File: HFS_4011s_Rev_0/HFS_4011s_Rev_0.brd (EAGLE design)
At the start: 47 x 44.5 mm, 15 parts, among them IC1 CP2104, J1 2X06, J2 2X12, Q1 mmbt2222, Q2 mmbt2222, SW2 KMR2, X2 ESP32_WROOM32_SKINNY, X4 20329

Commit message: Added power circuitry to board. Using 5V buck boost and 3.3V LDO. Added 1x02 pin header for on-off switch.
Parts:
- added B1: 1.8-5V, microbuilder:JSTPH2
- added C1: 10uF, microbuilder:0805-NO
- added C3: 2.2uF, microbuilder:0805-NO
- added C5: 0.1uF, microbuilder:0805-NO
- added C6: 10µF, microbuilder:0805-NO
- added C7: 100uF/6V, microbuilder:EIA3528-21/B-R
- added C8: 0.47uF, microbuilder:0603-NO
- added C9: 33uF, microbuilder:0603-NO
- added J3: 1X02, HFS4011sCustom:1X02
- added L1: VLC5045-6.8uH, microbuilder:INDUCTOR_5X5MM_TDK_VLC5045
- added LBO: RED, microbuilder:CHIPLED_0805_NOOUTLINE
- added LED3: ORANGE, microbuilder:CHIPLED_0805_NOOUTLINE
- added LED4: GREEN, microbuilder:CHIPLED_0805_NOOUTLINE
- added PWR: BLUE, microbuilder:CHIPLED_0805_NOOUTLINE
- added Q3: MMUN2133LT1G, transistor:SC59-BEC
- added R11, R2: 340K, microbuilder:0805-NO
- added R12, R4: 1.87Mohm, microbuilder:0805-NO
- added R20, R5, R7: 1K, microbuilder:0805-NO
- added R6: 470, microbuilder:0805-NO
- added R8: 2k, microbuilder:0805-NO
- added R9: 200K, microbuilder:0805-NO
- added U1: TPS61090RSAR, microbuilder:PVQFN-16
- added U2: MCP73831T-2ACI/OT, microbuilder:SOT23-5
- added U3: LM3940, HFS4011sCustom:SOT223
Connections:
- new net 5.0V: C3.1, C7.+, C8.1, PWR.A, R4.2, U1.1, U1.15, U1.16, U3.1
- new net ENABLE: J3.1, R2.2, U1.11
- new net LBO: Q3.B, U1.12
- new net N$1: LED3.C, R6.1
- new net N$10: PWR.C, R5.1
- new net N$11: R4.1, R9.2, U1.14
- new net N$14: LBO.A, R20.1
- new net N$15: Q3.C, R20.2
- new net N$3: L1.P$2, U1.3, U1.4
- new net N$4: R11.2, R12.1, U1.9
- new net N$7: R6.2, R7.2, U2.1
- new net N$8: R8.1, U2.5
- new net N$9: LED4.A, R7.1
- net 3.3V: now also C9.1, U3.3
- net GND: now also B1.1, C1.2, C3.2, C5.2, C6.2, C7.-, C8.2, C9.2, J3.2, LBO.C, LED4.C, R11.1, R5.2, R8.2, R9.1, U1.10, U1.13, U1.5, U1.6, U1.7, U1.P$18, U1.P$19, U1.P$20, U1.P$21, U1.P$22, U1.THERMAL, U2.2, U3.2, U3.4
- net VBAT: now also B1.2, C1.1, C5.1, L1.P$1, Q3.E, R12.2, R2.1, U1.8, U2.3
- net VBUS: now also C6.1, LED3.A, U2.4

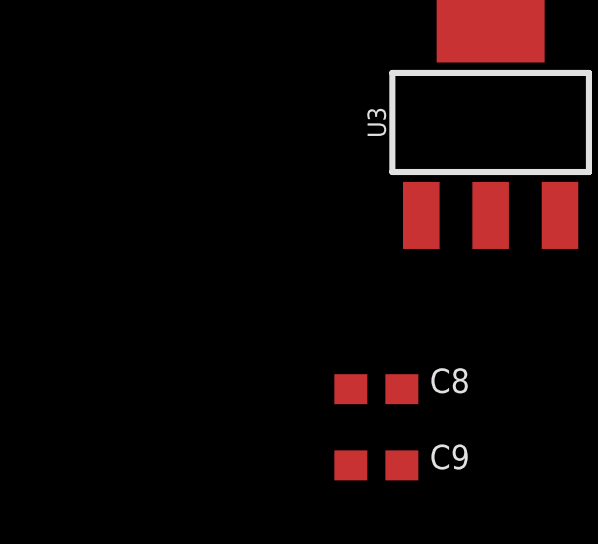
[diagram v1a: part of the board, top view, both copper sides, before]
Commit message: Added TVS diode on battery, and moved switch to battery.
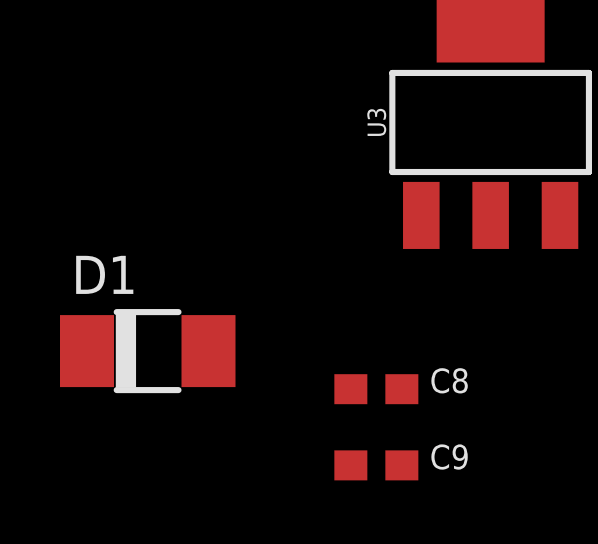
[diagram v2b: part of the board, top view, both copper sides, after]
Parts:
- added D1: SMAJ5.0CALFDKR-ND, HFS4011sCustom:DO-214AC
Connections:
- new net N$16: B1.2, J3.1
- net ENABLE: no longer J3.1
- net GND: now also D1.A; no longer J3.2
- net VBAT: now also D1.C, J3.2; no longer B1.2
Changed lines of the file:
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@@
 <element name="C8" library="microbuilder" package="0603-NO" value="0.47uF" x="2.54" y="-135.89"/>
 <element name="C9" library="microbuilder" package="0603-NO" value="33uF" x="2.54" y="-138.43"/>
+<element name="D1" library="HFS4011sCustom" package="DO-214AC" value="SMAJ5.0CALFDKR-ND" x="-5.08" y="-134.62"/>
 </elements>
 <signals>
@@
 <contactref element="R11" pad="1"/>
 <contactref element="LBO" pad="C"/>
-<contactref element="J3" pad="2"/>
 <contactref element="C8" pad="2"/>
 <contactref element="U3" pad="4"/>
 <contactref element="U3" pad="2"/>
 <contactref element="C9" pad="2"/>
-<wire x1="3.39" y1="-135.89" x2="3.39" y2="-138.43" width="0" layer="19" extent="1-1"/>
+<contactref element="D1" pad="A"/>
+<wire x1="3.39" y1="-135.89" x2="-3.055" y2="-134.62" width="0" layer="19" extent="1-1"/>
+<wire x1="3.39" y1="-138.43" x2="3.39" y2="-135.89" width="0" layer="19" extent="1-1"/>
 <wire x1="6.35" y1="-130.0988" x2="3.39" y2="-135.89" width="0" layer="19" extent="1-1"/>
 <wire x1="6.35" y1="-123.901" x2="6.35" y2="-130.0988" width="0" layer="19" extent="1-1"/>
-<wire x1="10.16" y1="-114.3" x2="6.35" y2="-123.901" width="0" layer="19" extent="1-1"/>
-<wire x1="9.84" y1="-104.14" x2="10.16" y2="-114.3" width="0" layer="19" extent="1-1"/>
+<wire x1="9.84" y1="-104.14" x2="6.35" y2="-123.901" width="0" layer="19" extent="1-1"/>
 <wire x1="16.19" y1="-104.14" x2="9.84" y2="-104.14" width="0" layer="19" extent="1-1"/>
 <wire x1="16.83" y1="-99.06" x2="16.19" y2="-104.14" width="0" layer="19" extent="1-1"/>
@@
 <contactref element="C5" pad="1"/>
 <contactref element="R12" pad="2"/>
-<contactref element="B1" pad="2"/>
 <contactref element="Q3" pad="E"/>
+<contactref element="J3" pad="2"/>
+<contactref element="D1" pad="C"/>
+<wire x1="10.16" y1="-114.3" x2="-7.105" y2="-134.62" width="0" layer="19" extent="1-1"/>
+<wire x1="7.94" y1="-104.14" x2="10.16" y2="-114.3" width="0" layer="19" extent="1-1"/>
 <wire x1="11.11" y1="-99.06" x2="7.94" y2="-104.14" width="0" layer="19" extent="1-1"/>
-<wire x1="6.08" y1="-91.33" x2="11.11" y2="-99.06" width="0" layer="19" extent="1-1"/>
-<wire x1="16.215" y1="-88.46" x2="6.08" y2="-91.33" width="0" layer="19" extent="1-1"/>
 <wire x1="20.64" y1="-104.14" x2="11.11" y2="-99.06" width="0" layer="19" extent="1-1"/>
 <wire x1="29.53" y1="-99.06" x2="20.64" y2="-104.14" width="0" layer="19" extent="1-1"/>
+<wire x1="16.215" y1="-88.46" x2="11.11" y2="-99.06" width="0" layer="19" extent="1-1"/>
 <wire x1="33.97" y1="-85.02" x2="29.53" y2="-99.06" width="0" layer="19" extent="1-1"/>
 <wire x1="33.96" y1="-71.12" x2="33.97" y2="-85.02" width="0" layer="19" extent="1-1"/>
@@
 <contactref element="R2" pad="2"/>
 <contactref element="U1" pad="11"/>
-<contactref element="J3" pad="1"/>
-<wire x1="31.43" y1="-99.06" x2="7.62" y2="-114.3" width="0" layer="19" extent="1-1"/>
 <wire x1="17.34" y1="-86.035" x2="31.43" y2="-99.06" width="0" layer="19" extent="1-1"/>
 </signal>
@@
 <wire x1="33.02" y1="-82.62" x2="25.08" y2="-99.06" width="0" layer="19" extent="1-1"/>
 </signal>
+<signal name="N$16">
+<contactref element="B1" pad="2"/>
+<contactref element="J3" pad="1"/>
+<wire x1="6.08" y1="-91.33" x2="7.62" y2="-114.3" width="0" layer="19" extent="1-1"/>
+</signal>
 </signals>

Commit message: Cleaned up schematic and added ground planes.
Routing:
- added copper zone on layer 1, net GND
- added copper zone on layer 16, net GND
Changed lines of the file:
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@@
 <contactref element="C9" pad="2"/>
 <contactref element="D1" pad="A"/>
+<polygon width="0.1524" layer="1">
+<vertex x="-7.62" y="49.53"/>
+<vertex x="53.34" y="49.53"/>
+<vertex x="53.34" y="-3.81"/>
+<vertex x="-7.62" y="-3.81"/>
+</polygon>
+<polygon width="0.1524" layer="16">
+<vertex x="-8.89" y="50.8"/>
+<vertex x="54.61" y="50.8"/>
+<vertex x="54.61" y="-5.08"/>
+<vertex x="-8.89" y="-5.08"/>
+</polygon>
 <wire x1="3.39" y1="-135.89" x2="-3.055" y2="-134.62" width="0" layer="19" extent="1-1"/>
 <wire x1="3.39" y1="-138.43" x2="3.39" y2="-135.89" width="0" layer="19" extent="1-1"/>
@@
 <wire x1="20.32" y1="-34.51" x2="9.84" y2="-36.83" width="0" layer="19" extent="1-1"/>
 <wire x1="22.11" y1="3.08" x2="20.32" y2="-34.51" width="0" layer="19" extent="1-1"/>
-<wire x1="23.61" y1="3.08" x2="22.11" y2="3.08" width="0" layer="19" extent="1-1"/>
-<wire x1="24.16" y1="5.855" x2="23.61" y2="3.08" width="0" layer="19" extent="1-1"/>
-<wire x1="26.16" y1="5.98" x2="24.16" y2="5.855" width="0" layer="19" extent="1-1"/>
+<wire x1="7.62" y1="30.48" x2="5.62" y2="31.23" width="0" layer="19" extent="1-1"/>
 <wire x1="26.46" y1="3.18" x2="26.16" y2="5.98" width="0" layer="19" extent="1-1"/>
-<wire x1="19.26" y1="3.18" x2="22.11" y2="3.08" width="0" layer="19" extent="1-1"/>
-<wire x1="19.56" y1="5.98" x2="19.26" y2="3.18" width="0" layer="19" extent="1-1"/>
-<wire x1="17.16" y1="11.23" x2="19.56" y2="5.98" width="0" layer="19" extent="1-1"/>
-<wire x1="23.2" y1="21.43" x2="17.16" y2="11.23" width="0" layer="19" extent="1-1"/>
-<wire x1="31.36" y1="29.13" x2="23.2" y2="21.43" width="0" layer="19" extent="1-1"/>
-<wire x1="14.36" y1="29.13" x2="23.2" y2="21.43" width="0" layer="19" extent="1-1"/>
-<wire x1="11.11" y1="25.4" x2="14.36" y2="29.13" width="0" layer="19" extent="1-1"/>
-<wire x1="8.4" y1="21.12" x2="11.11" y2="25.4" width="0" layer="19" extent="1-1"/>
-<wire x1="4.3" y1="21.12" x2="8.4" y2="21.12" width="0" layer="19" extent="1-1"/>
-<wire x1="7.62" y1="30.48" x2="11.11" y2="25.4" width="0" layer="19" extent="1-1"/>
-<wire x1="5.62" y1="31.23" x2="7.62" y2="30.48" width="0" layer="19" extent="1-1"/>
-<wire x1="1.69" y1="38.1" x2="5.62" y2="31.23" width="0" layer="19" extent="1-1"/>
-<wire x1="3.39" y1="41.91" x2="1.69" y2="38.1" width="0" layer="19" extent="1-1"/>
-<wire x1="7.62" y1="41.69" x2="3.39" y2="41.91" width="0" layer="19" extent="1-1"/>
+<wire x1="19.26" y1="3.18" x2="19.56" y2="5.98" width="0" layer="19" extent="1-1"/>
 </signal>
 <signal name="VBUS">
@@
 <contactref element="X2" pad="3"/>
 <contactref element="C4" pad="1"/>
-<wire x1="1.69" y1="41.91" x2="36.83" y2="34.12" width="0" layer="19" extent="1-1"/>
-<wire x1="8.02" y1="8.47" x2="1.69" y2="41.91" width="0" layer="19" extent="1-1"/>
-<wire x1="8.4" y1="19.52" x2="8.02" y2="8.47" width="0" layer="19" extent="1-1"/>
+<wire x1="14.36" y1="26.59" x2="36.83" y2="34.12" width="0" layer="19" extent="1-1"/>
+<wire x1="8.4" y1="19.52" x2="14.36" y2="26.59" width="0" layer="19" extent="1-1"/>
 <wire x1="4.3" y1="19.52" x2="8.4" y2="19.52" width="0" layer="19" extent="1-1"/>
-<wire x1="14.36" y1="26.59" x2="8.4" y2="19.52" width="0" layer="19" extent="1-1"/>
+<wire x1="8.02" y1="8.47" x2="8.4" y2="19.52" width="0" layer="19" extent="1-1"/>
+<wire x1="1.69" y1="41.91" x2="14.36" y2="26.59" width="0" layer="19" extent="1-1"/>
 </signal>
 <signal name="GPIO0">
@@
 <contactref element="X2" pad="34"/>
 <contactref element="IC1" pad="21"/>
-<wire x1="31.36" y1="24.05" x2="7.87" y2="32.48" width="0" layer="19" extent="1-1"/>
+<wire x1="7.87" y1="32.48" x2="31.36" y2="24.05" width="0" layer="19" extent="1-1"/>
 </signal>
 <signal name="TXD0">
 <contactref element="IC1" pad="20"/>
 <contactref element="X2" pad="35"/>
-<wire x1="31.36" y1="25.32" x2="8.37" y2="32.48" width="0" layer="19" extent="1-1"/>
+<wire x1="8.37" y1="32.48" x2="31.36" y2="25.32" width="0" layer="19" extent="1-1"/>
 </signal>
 <signal name="N$2">
 <contactref element="X4" pad="D+"/>
 <contactref element="IC1" pad="3"/>
-<wire x1="5.62" y1="30.73" x2="22.86" y2="5.855" width="0" layer="19" extent="1-1"/>
+<wire x1="22.86" y1="5.855" x2="5.62" y2="30.73" width="0" layer="19" extent="1-1"/>
 </signal>
 <signal name="N$6">
 <contactref element="X4" pad="D-"/>
 <contactref element="IC1" pad="4"/>
-<wire x1="5.62" y1="30.23" x2="22.21" y2="5.855" width="0" layer="19" extent="1-1"/>
+<wire x1="22.21" y1="5.855" x2="5.62" y2="30.23" width="0" layer="19" extent="1-1"/>
 </signal>
 <signal name="RTS">
@@
 <contactref element="X2" pad="16"/>
 <contactref element="R10" pad="1"/>
-<wire x1="8.04" y1="36.83" x2="18.43" y2="11.23" width="0" layer="19" extent="1-1"/>
+<wire x1="18.43" y1="11.23" x2="8.04" y2="36.83" width="0" layer="19" extent="1-1"/>
 </signal>
 <signal name="A2_I34">
@@
 <contactref element="R1" pad="1"/>
 <contactref element="R3" pad="2"/>
-<wire x1="3.39" y1="38.1" x2="4.23" y2="35.56" width="0" layer="19" extent="1-1"/>
-<wire x1="14.36" y1="21.51" x2="3.39" y2="38.1" width="0" layer="19" extent="1-1"/>
+<wire x1="4.23" y1="35.56" x2="3.39" y2="38.1" width="0" layer="19" extent="1-1"/>
+<wire x1="14.36" y1="21.51" x2="4.23" y2="35.56" width="0" layer="19" extent="1-1"/>
 </signal>
 <signal name="N$5">
